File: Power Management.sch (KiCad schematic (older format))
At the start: 22 parts, among them IC1 TLV809ED29DBZR, IC2 MAX17201G+T, Q4 Q_PMOS_GSD, U2 TPS61092, U3 LD1117S33TR_SOT223

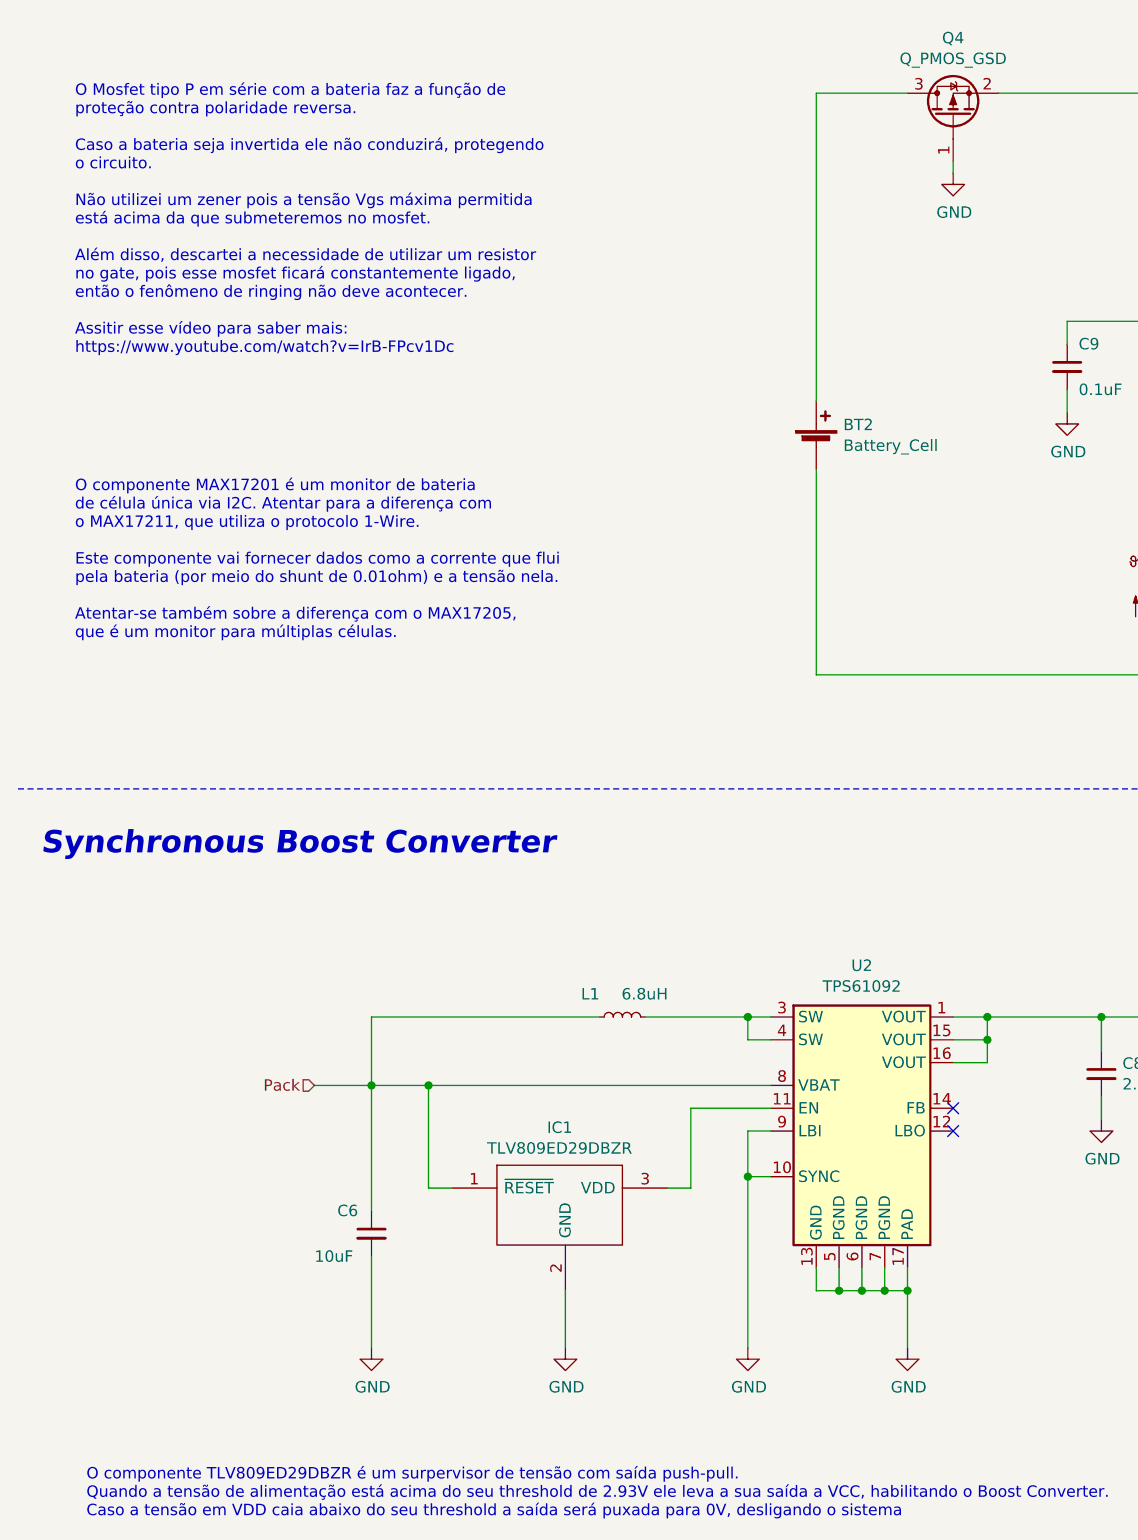
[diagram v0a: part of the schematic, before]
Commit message: Updated RF section ground planes.
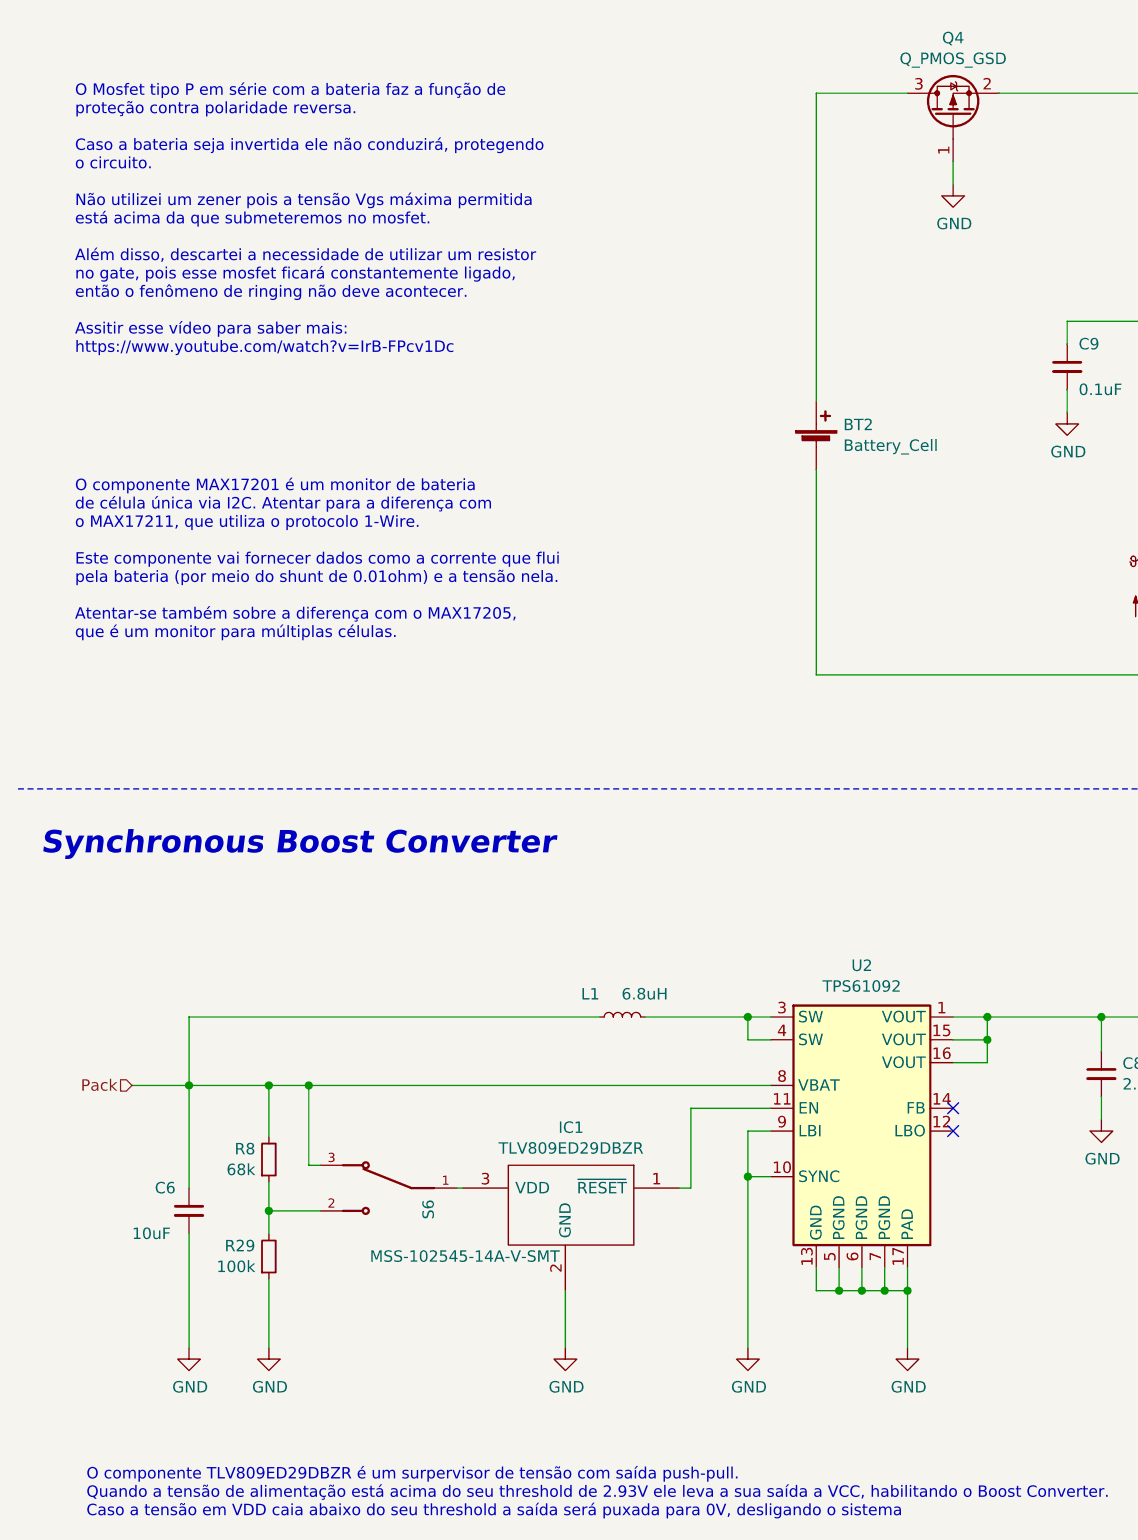
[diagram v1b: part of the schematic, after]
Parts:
- added R29: 100k, Resistor_SMD:R_0603_1608Metric, symbol Device:R_Small
- added R8: 68k, Resistor_SMD:R_0603_1608Metric, symbol Device:R_Small
- added S6: MSS-102545-14A-V-SMT, SW_MSS-102545-14A-V-SMT, symbol MSS-102545-14A-V-SMT:MSS-102545-14A-V-SMT
- C10: footprint Capacitor_SMD:CP_Elec_5x3 -> Capacitor_SMD:CP_Elec_5x5.3
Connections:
- net GND: now also R29.1
- net Pack: now also R8.2, S6.3; no longer IC1.1 (~RESET)
- net at U2.11 (EN): now also IC1.1 (~RESET); no longer IC1.3 (VDD)
- new net: IC1.3 (VDD), S6.1
- new net: R29.2, R8.1, S6.2
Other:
- moved on the sheet: C6, IC1
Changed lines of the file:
@@
 L Device:C_Small C6
 U 1 1 60E78225
-P 2050 6300
-F 0 "C6" H 1900 6400 50  0000 L CNN
-F 1 "10uF" H 1800 6200 50  0000 L CNN
-F 2 "Capacitor_SMD:C_1206_3216Metric" H 2050 6300 50  0001 C CNN
-F 3 "~" H 2050 6300 50  0001 C CNN
-	1    2050 6300
+P 1250 6200
+F 0 "C6" H 1100 6300 50  0000 L CNN
+F 1 "10uF" H 1000 6100 50  0000 L CNN
+F 2 "Capacitor_SMD:C_1206_3216Metric" H 1250 6200 50  0001 C CNN
+F 3 "~" H 1250 6200 50  0001 C CNN
+	1    1250 6200
 	1    0    0    -1
 $EndComp
@@
 F 0 "C10" H 5788 5646 50  0000 L CNN
 F 1 "100uF" H 5788 5555 50  0000 L CNN
-F 2 "Capacitor_SMD:CP_Elec_5x3" H 5700 5600 50  0001 C CNN
+F 2 "Capacitor_SMD:CP_Elec_5x5.3" H 5700 5600 50  0001 C CNN
 F 3 "~" H 5700 5600 50  0001 C CNN
 	1    5700 5600
@@
 L power:GND #PWR0108
 U 1 1 610FCF6D
-P 4600 1650
-F 0 "#PWR0108" H 4600 1400 50  0001 C CNN
-F 1 "GND" H 4605 1477 50  0000 C CNN
-F 2 "" H 4600 1650 50  0001 C CNN
-F 3 "" H 4600 1650 50  0001 C CNN
-	1    4600 1650
-	1    0    0    -1
-$EndComp
-Wire Wire Line
-	4600 1650 4600 1600
+P 4600 1700
+F 0 "#PWR0108" H 4600 1450 50  0001 C CNN
+F 1 "GND" H 4605 1527 50  0000 C CNN
+F 2 "" H 4600 1700 50  0001 C CNN
+F 3 "" H 4600 1700 50  0001 C CNN
+	1    4600 1700
+	1    0    0    -1
+$EndComp
 $Comp
 L Regulator_Switching:TPS61092 U2
@@
 $EndComp
 Wire Wire Line
-	2050 6200 2050 5650
-Text HLabel 1800 5650 0    50   Input ~ 0
-Pack
-Connection ~ 2050 5650
-Wire Wire Line
-	1800 5650 2050 5650
+	1250 6100 1250 5650
+Connection ~ 1250 5650
+Wire Wire Line
+	1000 5650 1250 5650
 $Comp
 L Device:L_Small L1
@@
 Connection ~ 3700 5350
 Wire Wire Line
-	2050 5650 2300 5650
-Wire Wire Line
-	3050 5350 2050 5350
-Wire Wire Line
-	2050 5350 2050 5650
+	1250 5350 1250 5650
 $Comp
 L power:GND #PWR0109
 U 1 1 612ACFAF
-P 2050 6800
-F 0 "#PWR0109" H 2050 6550 50  0001 C CNN
-F 1 "GND" H 2055 6627 50  0000 C CNN
-F 2 "" H 2050 6800 50  0001 C CNN
-F 3 "" H 2050 6800 50  0001 C CNN
-	1    2050 6800
+P 1250 6800
+F 0 "#PWR0109" H 1250 6550 50  0001 C CNN
+F 1 "GND" H 1255 6627 50  0000 C CNN
+F 2 "" H 1250 6800 50  0001 C CNN
+F 3 "" H 1250 6800 50  0001 C CNN
+	1    1250 6800
 	1    0    0    -1
 $EndComp
@@
 	3700 6050 3700 6800
 Wire Wire Line
-	2050 6400 2050 6800
-Wire Wire Line
-	2400 6100 2300 6100
-Wire Wire Line
-	2300 6100 2300 5650
-Connection ~ 2300 5650
-Wire Wire Line
-	2300 5650 3800 5650
-Wire Wire Line
-	3350 6100 3450 6100
+	1250 6300 1250 6800
 Wire Wire Line
 	3450 6100 3450 5750
@@
 L SamacSys_Parts:TLV809ED29DBZR IC1
 U 1 1 612EBEE6
-P 2400 6200
-F 0 "IC1" H 2875 6565 50  0000 C CNN
-F 1 "TLV809ED29DBZR" H 2875 6474 50  0000 C CNN
-F 2 "SamacSys_Parts:SOT95P237X112-3N" H 3450 6300 50  0001 L CNN
-F 3 "https://www.ti.com/lit/ds/symlink/tlv809e.pdf?ts=1623232092527&ref_url=https%253A%252F%252Fwww.ti.com%252Fproduct%252FTLV809E%253FkeyMatch%253DTLV809EF30DBZR%2526tisearch%253Dsearch-everything%2526usecase%253DOPN" H 3450 6200 50  0001 L CNN
-F 4 "Supervisory Circuits Low-power voltage supervisor (reset IC) with active-low, push-pull output 3-SOT-23 -40 to 125" H 3450 6100 50  0001 L CNN "Description"
-F 5 "1.12" H 3450 6000 50  0001 L CNN "Height"
-F 6 "595-TLV809ED29DBZR" H 3450 5900 50  0001 L CNN "Mouser Part Number"
-F 7 "https://www.mouser.co.uk/ProductDetail/Texas-Instruments/TLV809ED29DBZR?qs=CiayqK2gdcJa0MXo3ZjyIg%3D%3D" H 3450 5800 50  0001 L CNN "Mouser Price/Stock"
-F 8 "Texas Instruments" H 3450 5700 50  0001 L CNN "Manufacturer_Name"
-F 9 "TLV809ED29DBZR" H 3450 5600 50  0001 L CNN "Manufacturer_Part_Number"
-	1    2400 6200
-	1    0    0    -1
+P 3400 6200
+F 0 "IC1" H 3875 6565 50  0000 C CNN
+F 1 "TLV809ED29DBZR" H 3875 6474 50  0000 C CNN
+F 2 "SamacSys_Parts:SOT95P237X112-3N" H 4450 6300 50  0001 L CNN
+F 3 "https://www.ti.com/lit/ds/symlink/tlv809e.pdf?ts=1623232092527&ref_url=https%253A%252F%252Fwww.ti.com%252Fproduct%252FTLV809E%253FkeyMatch%253DTLV809EF30DBZR%2526tisearch%253Dsearch-everything%2526usecase%253DOPN" H 4450 6200 50  0001 L CNN
+F 4 "Supervisory Circuits Low-power voltage supervisor (reset IC) with active-low, push-pull output 3-SOT-23 -40 to 125" H 4450 6100 50  0001 L CNN "Description"
+F 5 "1.12" H 4450 6000 50  0001 L CNN "Height"
+F 6 "595-TLV809ED29DBZR" H 4450 5900 50  0001 L CNN "Mouser Part Number"
+F 7 "https://www.mouser.co.uk/ProductDetail/Texas-Instruments/TLV809ED29DBZR?qs=CiayqK2gdcJa0MXo3ZjyIg%3D%3D" H 4450 5800 50  0001 L CNN "Mouser Price/Stock"
+F 8 "Texas Instruments" H 4450 5700 50  0001 L CNN "Manufacturer_Name"
+F 9 "TLV809ED29DBZR" H 4450 5600 50  0001 L CNN "Manufacturer_Part_Number"
+	1    3400 6200
+	-1   0    0    -1
 $EndComp
 $Comp
@@
 Text Notes 750  3700 0    50   ~ 0
 O componente MAX17201 é um monitor de bateria\nde célula única via I2C. Atentar para a diferença com\no MAX17211, que utiliza o protocolo 1-Wire.\n\nEste componente vai fornecer dados como a corrente que flui\npela bateria (por meio do shunt de 0.01ohm) e a tensão nela.\n\nAtentar-se também sobre a diferença com o MAX17205,\nque é um monitor para múltiplas células.
+Wire Wire Line
+	4600 1600 4600 1700
+$Comp
+L MSS-102545-14A-V-SMT:MSS-102545-14A-V-SMT S6
+U 1 1 6196346E
+P 2125 6100
+F 0 "S6" V 1950 6150 50  0000 L CNN
+F 1 "MSS-102545-14A-V-SMT" H 1375 6400 50  0000 L CNN
+F 2 "SW_MSS-102545-14A-V-SMT" H 2125 6100 50  0001 L BNN
+F 3 "" H 2125 6100 50  0001 L BNN
+F 4 "Manufacturer Recommendations" H 2125 6100 50  0001 L BNN "STANDARD"
+F 5 "1.0" H 2125 6100 50  0001 L BNN "PARTREV"
+F 6 "CUI Devices" H 2125 6100 50  0001 L BNN "MANUFACTURER"
+F 7 "2.7 mm" H 2125 6100 50  0001 L BNN "MAXIMUM_PACKAGE_HEIGHT"
+	1    2125 6100
+	-1   0    0    1
+$EndComp
+Text HLabel 1000 5650 0    50   Input ~ 0
+Pack
+Wire Wire Line
+	1250 5350 3050 5350
+Wire Wire Line
+	1250 5650 1600 5650
+Wire Wire Line
+	1825 6000 1775 6000
+Wire Wire Line
+	1775 6000 1775 5650
+Connection ~ 1775 5650
+Wire Wire Line
+	1775 5650 3800 5650
+$Comp
+L Device:R_Small R?
+U 1 1 61991C9D
+P 1600 5975
+AR Path="/61991C9D" Ref="R?"  Part="1"
+AR Path="/60D72946/61991C9D" Ref="R8"  Part="1"
+F 0 "R8" H 1541 5929 50  0000 R CNN
+F 1 "68k" H 1541 6020 50  0000 R CNN
+F 2 "Resistor_SMD:R_0603_1608Metric" H 1600 5975 50  0001 C CNN
+F 3 "~" H 1600 5975 50  0001 C CNN
+	1    1600 5975
+	1    0    0    1
+$EndComp
+Wire Wire Line
+	1600 5875 1600 5650
+Connection ~ 1600 5650
+Wire Wire Line
+	1600 5650 1775 5650
+Wire Wire Line
+	1600 6075 1600 6200
+Wire Wire Line
+	1600 6200 1825 6200
+$Comp
+L Device:R_Small R?
+U 1 1 6199CCDA
+P 1600 6400
+AR Path="/6199CCDA" Ref="R?"  Part="1"
+AR Path="/60D72946/6199CCDA" Ref="R29"  Part="1"
+F 0 "R29" H 1541 6354 50  0000 R CNN
+F 1 "100k" H 1541 6445 50  0000 R CNN
+F 2 "Resistor_SMD:R_0603_1608Metric" H 1600 6400 50  0001 C CNN
+F 3 "~" H 1600 6400 50  0001 C CNN
+	1    1600 6400
+	1    0    0    1
+$EndComp
+Wire Wire Line
+	1600 6300 1600 6200
+Connection ~ 1600 6200
+$Comp
+L power:GND #PWR0106
+U 1 1 619A465D
+P 1600 6800
+F 0 "#PWR0106" H 1600 6550 50  0001 C CNN
+F 1 "GND" H 1605 6627 50  0000 C CNN
+F 2 "" H 1600 6800 50  0001 C CNN
+F 3 "" H 1600 6800 50  0001 C CNN
+	1    1600 6800
+	1    0    0    -1
+$EndComp
+Wire Wire Line
+	1600 6800 1600 6500
+Wire Wire Line
+	3450 6100 3400 6100
+Wire Wire Line
+	2425 6100 2450 6100
 $EndSCHEMATC
